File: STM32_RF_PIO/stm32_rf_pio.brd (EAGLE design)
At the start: 80 x 39.4 mm, 10 parts, among them IC1 ULN2804A, IC2 ULN2804A, IC3 ULN2804A, X1 22-23-2081, X2 22-23-2081, X3 22-23-2081, X4 Outputs Power

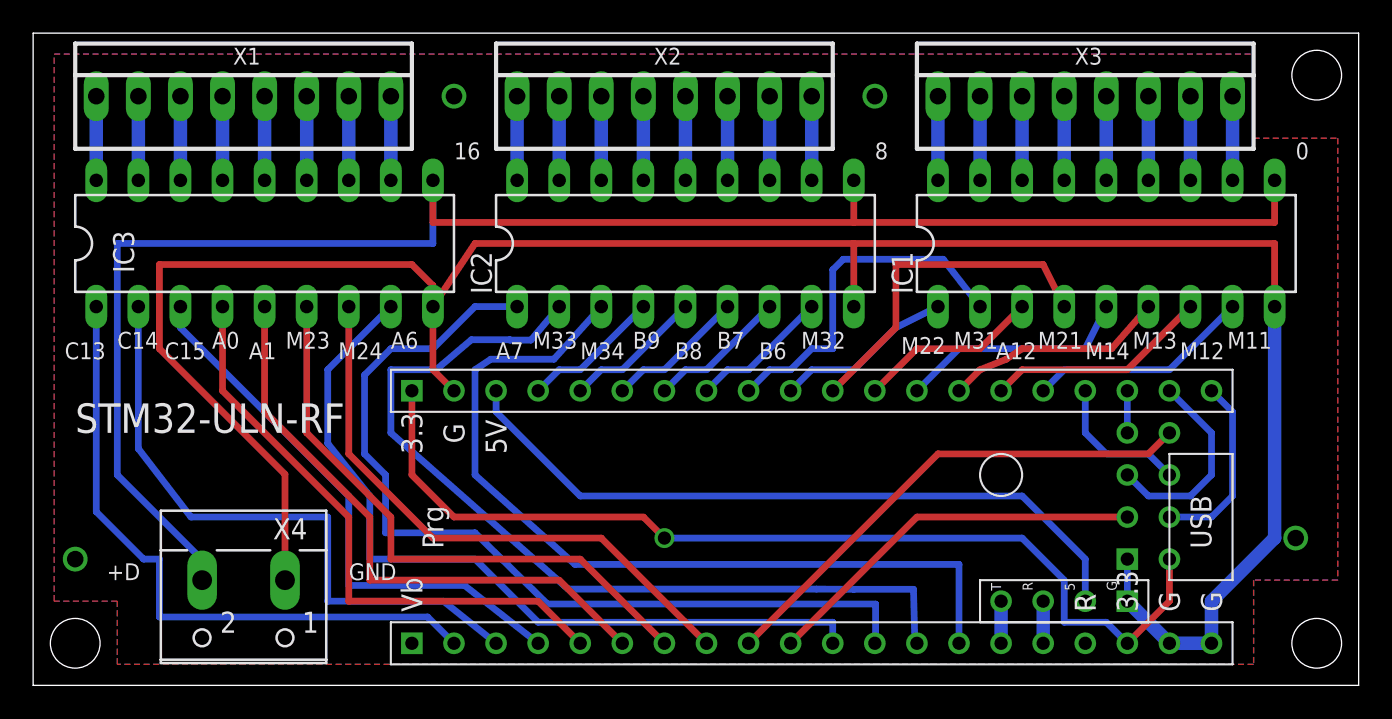
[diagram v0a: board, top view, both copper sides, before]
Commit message: Added connections for servo motors with Gnd-HV-Signal for all pwm outputs
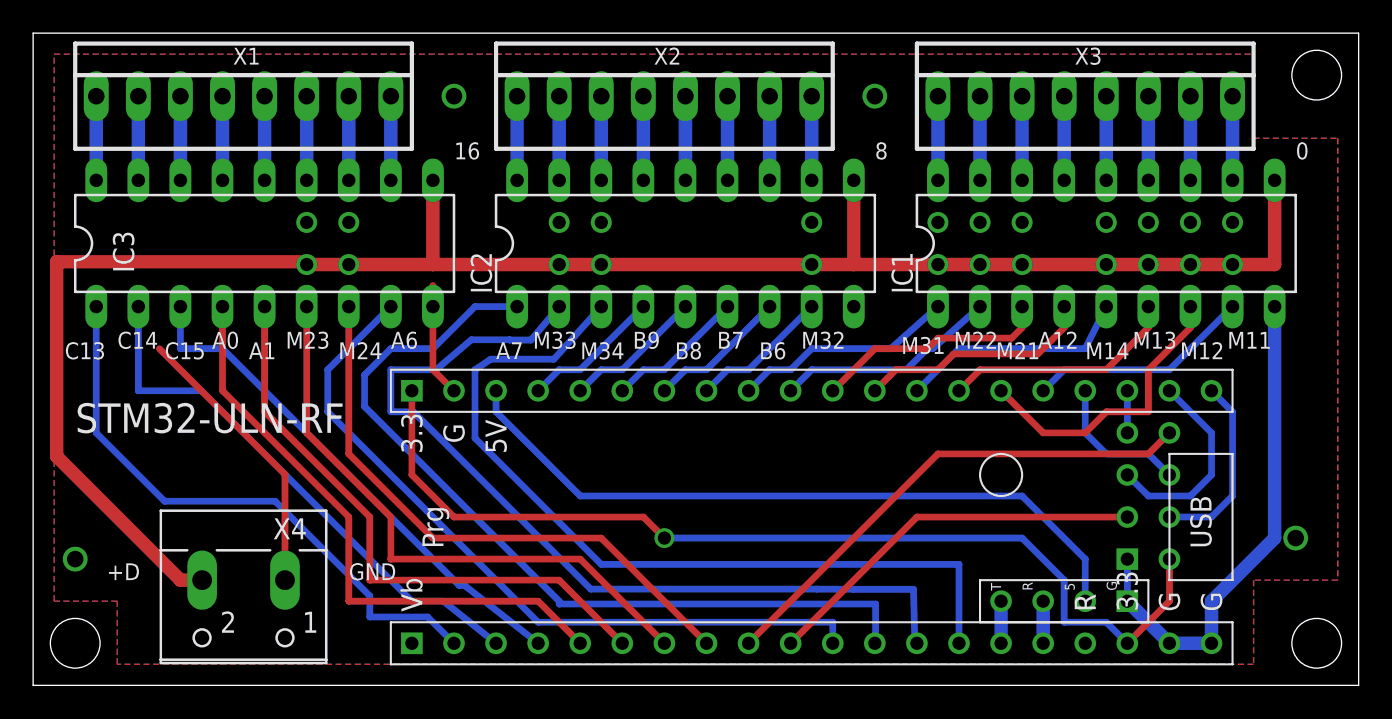
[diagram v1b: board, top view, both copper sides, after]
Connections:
- net N$53 renamed HV
- net A12: now also IC1.4; no longer IC1.3
- net M21: now also IC1.3; no longer IC1.4
- net M22: now also IC1.2; no longer IC1.1
- net M31: now also IC1.1; no longer IC1.2
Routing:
- net GND: track 137.1 -> 54.6 mm, vias 0 -> 16
- net HV: track 103.7 -> 120.1 mm, vias 0 -> 12
- net M31: track 21.4 -> 13.4 mm
- net M21: track 20.9 -> 14.3 mm
- net N$30: track 38.2 -> 32.8 mm
- net M12: track 13.5 -> 17.9 mm
- net N$29: track 39.3 -> 35.2 mm
- net N$20: track 54.7 -> 51.1 mm
- net N$28: track 48.5 -> 44.9 mm
- net A12: track 11.0 -> 14.3 mm
- net M22: track 10.8 -> 13.4 mm
- net N$31: track 33.7 -> 31.3 mm
- net M34: track 51.6 -> 50.5 mm
- net M13: track 13.4 -> 14.3 mm

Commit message: gnd with rastnet
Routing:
- net GND: track 54.6 -> 37.4 mm
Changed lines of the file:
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@@
 <wire x1="71.12" y1="2.54" x2="68.58" y2="2.54" width="0.8128" layer="16"/>
 <wire x1="68.58" y1="2.54" x2="66.04" y2="5.08" width="0.8128" layer="16"/>
-<wire x1="15.2" y1="6.35" x2="15.2" y2="12.74" width="0.4064" layer="1"/>
-<wire x1="15.2" y1="12.74" x2="7.62" y2="20.32" width="0.4064" layer="1"/>
 <wire x1="24.13" y1="24.13" x2="24.13" y2="22.86" width="0.4064" layer="1"/>
 <wire x1="74.93" y1="22.86" x2="74.93" y2="8.89" width="0.8128" layer="16"/>
@@
 <via x="69.85" y="27.94" extent="1-16" drill="0.8" diameter="1.27" shape="square"/>
 <via x="72.39" y="27.94" extent="1-16" drill="0.8" diameter="1.27" shape="square"/>
-<wire x1="69.85" y1="27.94" x2="72.39" y2="27.94" width="0" layer="19" extent="1-1"/>
 </signal>
 <signal name="3V3">

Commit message: preparing production 1
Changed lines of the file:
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@@
 <layers>
 <layer number="1" name="Top" color="4" fill="1" visible="yes" active="yes"/>
-<layer number="16" name="Bottom" color="1" fill="1" visible="no" active="yes"/>
+<layer number="16" name="Bottom" color="1" fill="1" visible="yes" active="yes"/>
 <layer number="17" name="Pads" color="2" fill="1" visible="yes" active="yes"/>
 <layer number="18" name="Vias" color="2" fill="1" visible="yes" active="yes"/>
@@
 <layer number="20" name="Dimension" color="15" fill="1" visible="yes" active="yes"/>
 <layer number="21" name="tPlace" color="7" fill="1" visible="yes" active="yes"/>
-<layer number="22" name="bPlace" color="7" fill="1" visible="no" active="yes"/>
+<layer number="22" name="bPlace" color="7" fill="1" visible="yes" active="yes"/>
 <layer number="23" name="tOrigins" color="15" fill="1" visible="yes" active="yes"/>
-<layer number="24" name="bOrigins" color="15" fill="1" visible="no" active="yes"/>
+<layer number="24" name="bOrigins" color="15" fill="1" visible="yes" active="yes"/>
 <layer number="25" name="tNames" color="7" fill="1" visible="yes" active="yes"/>
-<layer number="26" name="bNames" color="7" fill="1" visible="no" active="yes"/>
+<layer number="26" name="bNames" color="7" fill="1" visible="yes" active="yes"/>
 <layer number="27" name="tValues" color="7" fill="1" visible="yes" active="yes"/>
-<layer number="28" name="bValues" color="7" fill="1" visible="no" active="yes"/>
+<layer number="28" name="bValues" color="7" fill="1" visible="yes" active="yes"/>
 <layer number="29" name="tStop" color="7" fill="3" visible="no" active="yes"/>
 <layer number="30" name="bStop" color="7" fill="6" visible="no" active="yes"/>
@@
 </class>
 </classes>
-<designrules name="default">
+<designrules name="EagleRules">
 <description language="de">&lt;b&gt;EAGLE Design Rules&lt;/b&gt;
 &lt;p&gt;
@@
 necessary adjustments and save your customized
 design rules under a new name.</description>
+<description language="zh">&lt;b&gt;NOA-Labs EAGLE Design Rules&lt;/b&gt;
+</description>
 <param name="layerSetup" value="(1*16)"/>
 <param name="mtCopper" value="0.035mm 0.035mm 0.035mm 0.035mm 0.035mm 0.035mm 0.035mm 0.035mm 0.035mm 0.035mm 0.035mm 0.035mm 0.035mm 0.035mm 0.035mm 0.035mm"/>
 <param name="mtIsolate" value="1.5mm 0.15mm 0.2mm 0.15mm 0.2mm 0.15mm 0.2mm 0.15mm 0.2mm 0.15mm 0.2mm 0.15mm 0.2mm 0.15mm 0.2mm"/>
-<param name="mdWireWire" value="8mil"/>
-<param name="mdWirePad" value="8mil"/>
-<param name="mdWireVia" value="8mil"/>
-<param name="mdPadPad" value="8mil"/>
-<param name="mdPadVia" value="8mil"/>
-<param name="mdViaVia" value="8mil"/>
-<param name="mdSmdPad" value="8mil"/>
-<param name="mdSmdVia" value="8mil"/>
-<param name="mdSmdSmd" value="8mil"/>
+<param name="mdWireWire" value="7mil"/>
+<param name="mdWirePad" value="7mil"/>
+<param name="mdWireVia" value="7mil"/>
+<param name="mdPadPad" value="7mil"/>
+<param name="mdPadVia" value="7mil"/>
+<param name="mdViaVia" value="7mil"/>
+<param name="mdSmdPad" value="0mil"/>
+<param name="mdSmdVia" value="0mil"/>
+<param name="mdSmdSmd" value="0mil"/>
 <param name="mdViaViaSameLayer" value="8mil"/>
 <param name="mnLayersViaInSmd" value="2"/>
-<param name="mdCopperDimension" value="40mil"/>
-<param name="mdDrill" value="8mil"/>
+<param name="mdCopperDimension" value="20mil"/>
+<param name="mdDrill" value="10mil"/>
 <param name="mdSmdStop" value="0mil"/>
-<param name="msWidth" value="10mil"/>
-<param name="msDrill" value="24mil"/>
-<param name="msMicroVia" value="9.99mm"/>
+<param name="msWidth" value="7mil"/>
+<param name="msDrill" value="12mil"/>
+<param name="msMicroVia" value="12mil"/>
 <param name="msBlindViaRatio" value="0.5"/>
 <param name="rvPadTop" value="0.25"/>
@@
 <param name="rlMinPadBottom" value="10mil"/>
 <param name="rlMaxPadBottom" value="20mil"/>
-<param name="rlMinViaOuter" value="8mil"/>
+<param name="rlMinViaOuter" value="6mil"/>
 <param name="rlMaxViaOuter" value="20mil"/>
-<param name="rlMinViaInner" value="8mil"/>
+<param name="rlMinViaInner" value="6mil"/>
 <param name="rlMaxViaInner" value="20mil"/>
 <param name="rlMinMicroViaOuter" value="4mil"/>
@@
 <param name="psTop" value="-1"/>
 <param name="psBottom" value="-1"/>
-<param name="psFirst" value="-1"/>
+<param name="psFirst" value="0"/>
 <param name="psElongationLong" value="100"/>
 <param name="psElongationOffset" value="100"/>
 <param name="mvStopFrame" value="1"/>
 <param name="mvCreamFrame" value="0"/>
-<param name="mlMinStopFrame" value="4mil"/>
-<param name="mlMaxStopFrame" value="4mil"/>
+<param name="mlMinStopFrame" value="2mil"/>
+<param name="mlMaxStopFrame" value="2mil"/>
 <param name="mlMinCreamFrame" value="0mil"/>
 <param name="mlMaxCreamFrame" value="0mil"/>
-<param name="mlViaStopLimit" value="0mil"/>
+<param name="mlViaStopLimit" value="25mil"/>
 <param name="srRoundness" value="0"/>
 <param name="srMinRoundness" value="0mil"/>
@@
 <param name="checkAngle" value="0"/>
 <param name="checkFont" value="1"/>
-<param name="checkRestrict" value="1"/>
+<param name="checkRestrict" value="0"/>
 <param name="useDiameter" value="13"/>
 <param name="maxErrors" value="50"/>
